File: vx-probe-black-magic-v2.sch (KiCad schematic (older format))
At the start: 23 parts, among them P1 USB MINI B, U1 stm32f070-qfp48, U2 AT45DB321D-SU, Y1 8 MHz

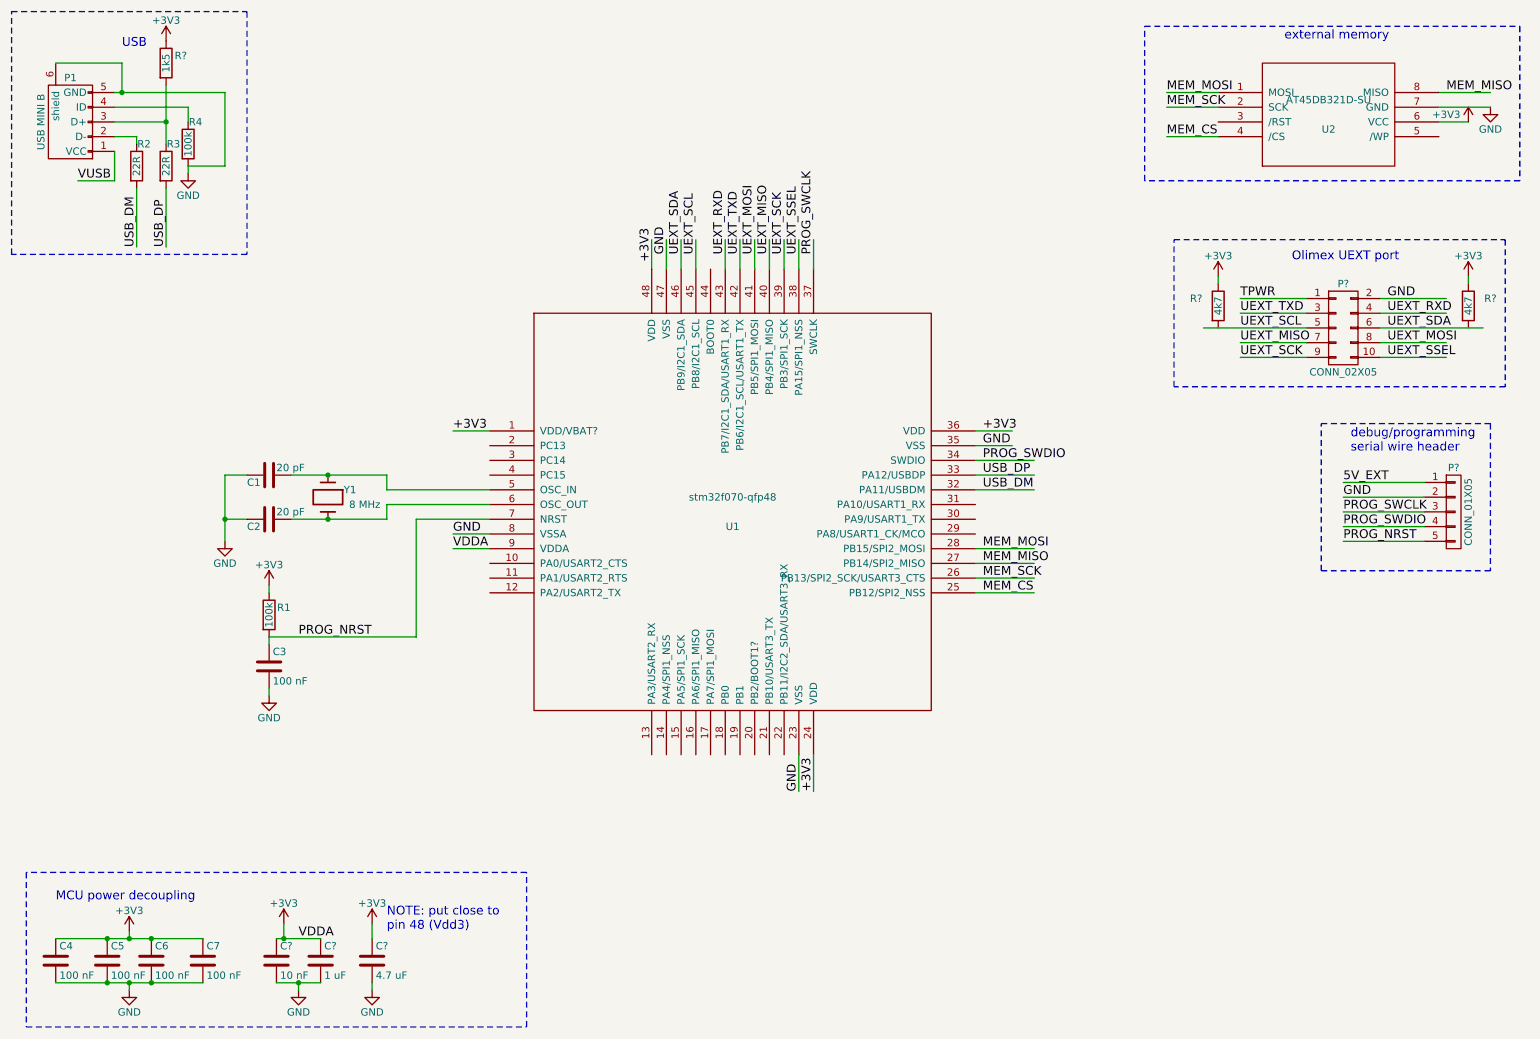
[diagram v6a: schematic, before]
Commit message: added boot selection setup
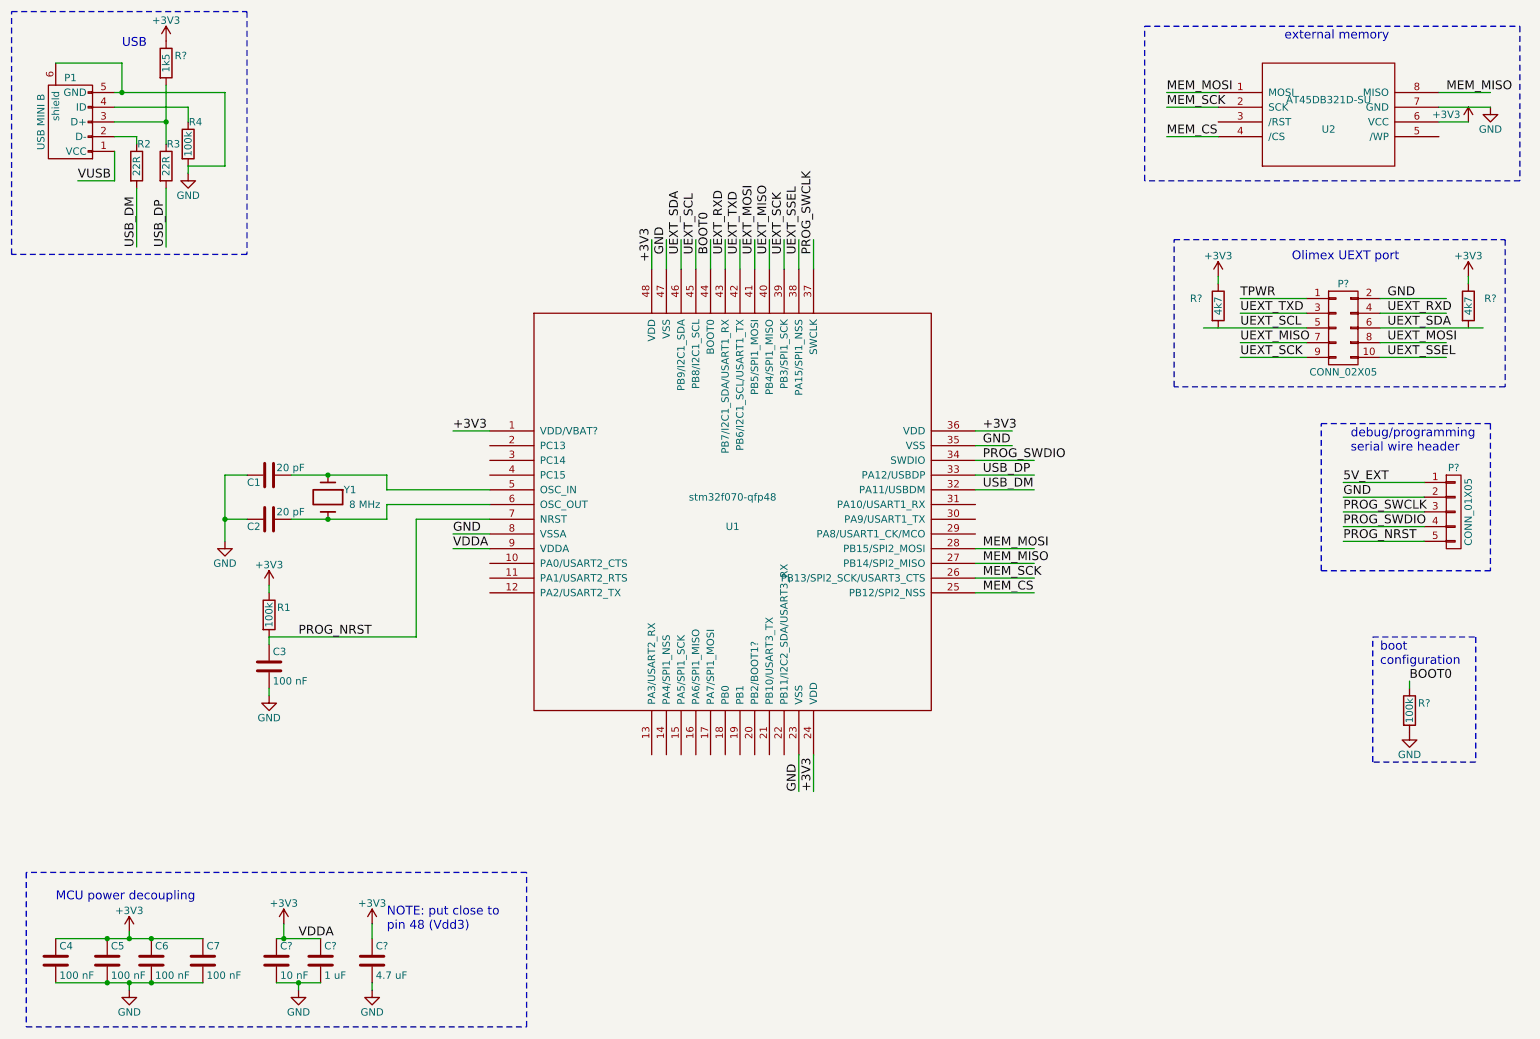
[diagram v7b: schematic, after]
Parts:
- added R?: 100k, symbol R
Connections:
- net labels added: BOOT0
- wire segments 89 -> 91
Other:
- note added: "boot\nconfiguration"
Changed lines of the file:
@@
 Wire Notes Line
 	9650 4400 9650 3400
+Wire Wire Line
+	5500 2350 5500 2150
+Text Label 5500 2250 1    60   ~ 0
+BOOT0
+Text Notes 10050 5050 0    60   ~ 0
+boot\nconfiguration
+Wire Wire Line
+	10250 5150 10250 5200
+$Comp
+L R R?
+U 1 1 57D8D839
+P 10250 5350
+F 0 "R?" H 10350 5400 50  0000 C CNN
+F 1 "100k" V 10250 5350 50  0000 C CNN
+F 2 "" V 10180 5350 50  0000 C CNN
+F 3 "" H 10250 5350 50  0000 C CNN
+	1    10250 5350
+	1    0    0    -1
+$EndComp
+$Comp
+L GND #PWR?
+U 1 1 57D8DA47
+P 10250 5500
+F 0 "#PWR?" H 10250 5250 50  0001 C CNN
+F 1 "GND" H 10250 5350 50  0000 C CNN
+F 2 "" H 10250 5500 50  0000 C CNN
+F 3 "" H 10250 5500 50  0000 C CNN
+	1    10250 5500
+	1    0    0    -1
+$EndComp
+Text Label 10250 5150 0    60   ~ 0
+BOOT0
+Wire Notes Line
+	10000 4850 10700 4850
+Wire Notes Line
+	10700 4850 10700 5700
+Wire Notes Line
+	10700 5700 10000 5700
+Wire Notes Line
+	10000 5700 10000 4850
 $EndSCHEMATC

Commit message: added power supply block
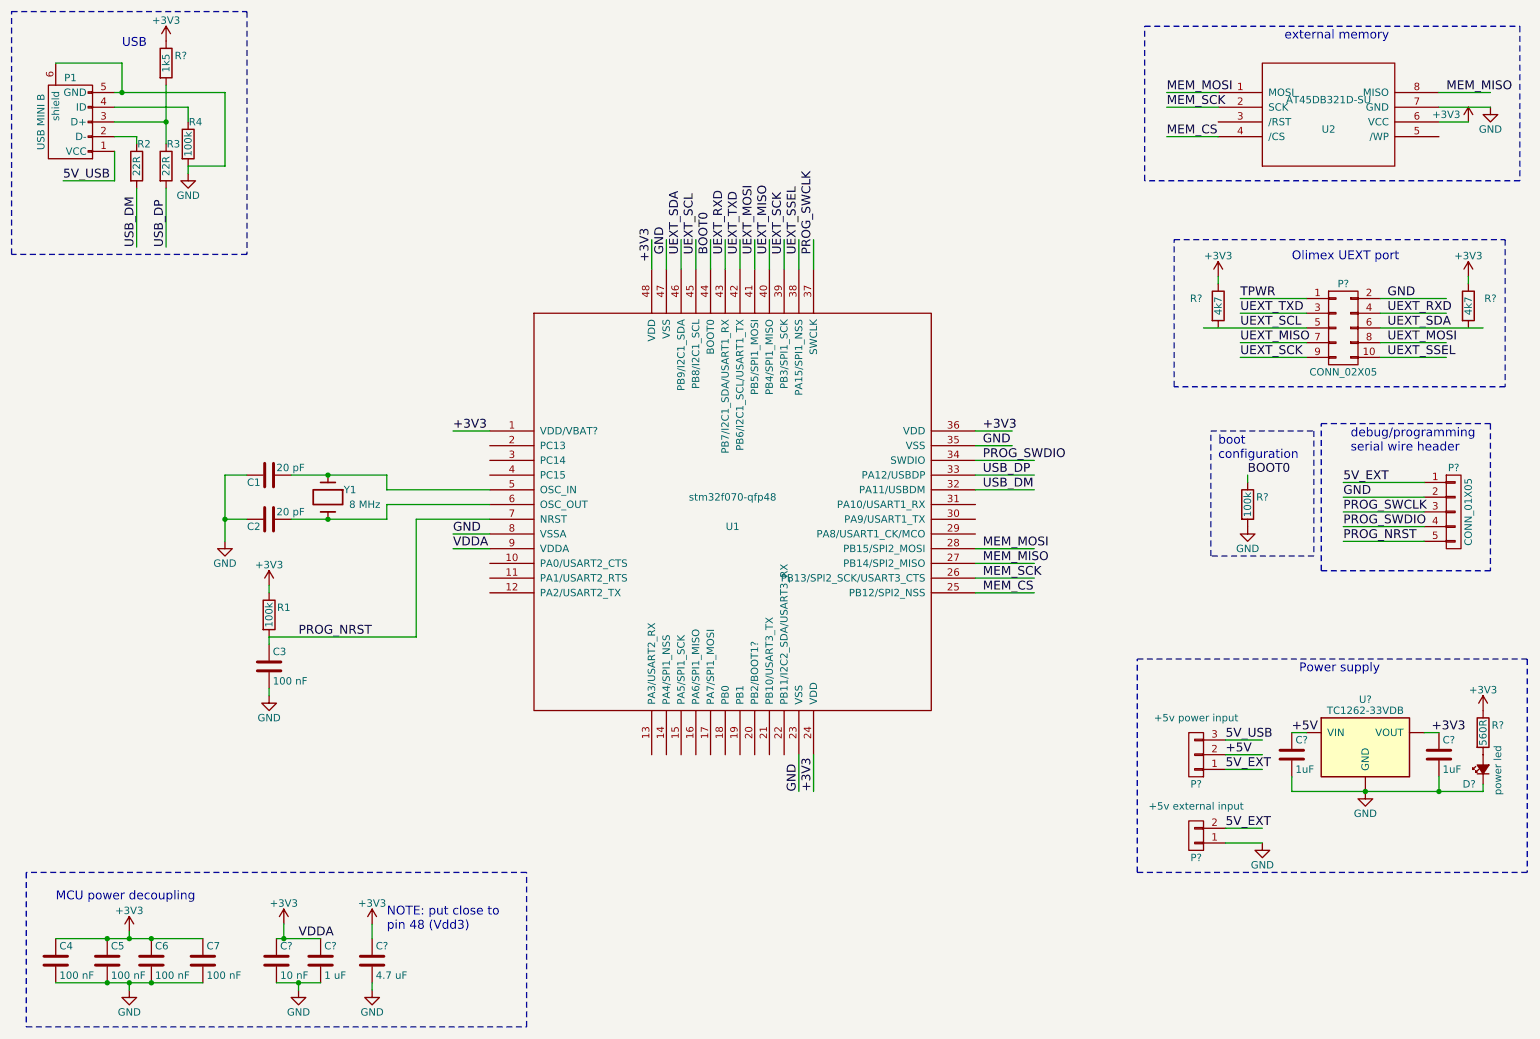
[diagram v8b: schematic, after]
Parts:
- added C? (x2): 1uF, symbol C
- added D?: power led, symbol Led_Small
- added P?: +5v power input, symbol CONN_01X03
- added P?: +5v external input, symbol CONN_01X02
- added R?: 560R, symbol R
- added U?: TC1262-33VDB, SOT-223, symbol TC1262-33VDB
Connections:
- net labels added: +5V, 5V_USB
- net labels removed: VUSB
- wire segments 91 -> 102
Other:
- note added: "Power supply"
- moved on the sheet: R?
